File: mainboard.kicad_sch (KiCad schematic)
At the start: 29 parts, among them J1 terminal_led-strip, J2 header_rotary-encoder, J4 header_pi, J5 power_input, J6 AudioJack2, Q1 IRF9540N, SW1 power_switch, U1 OPA2277, U2 MSGEQ7, U4 logic-level-converter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

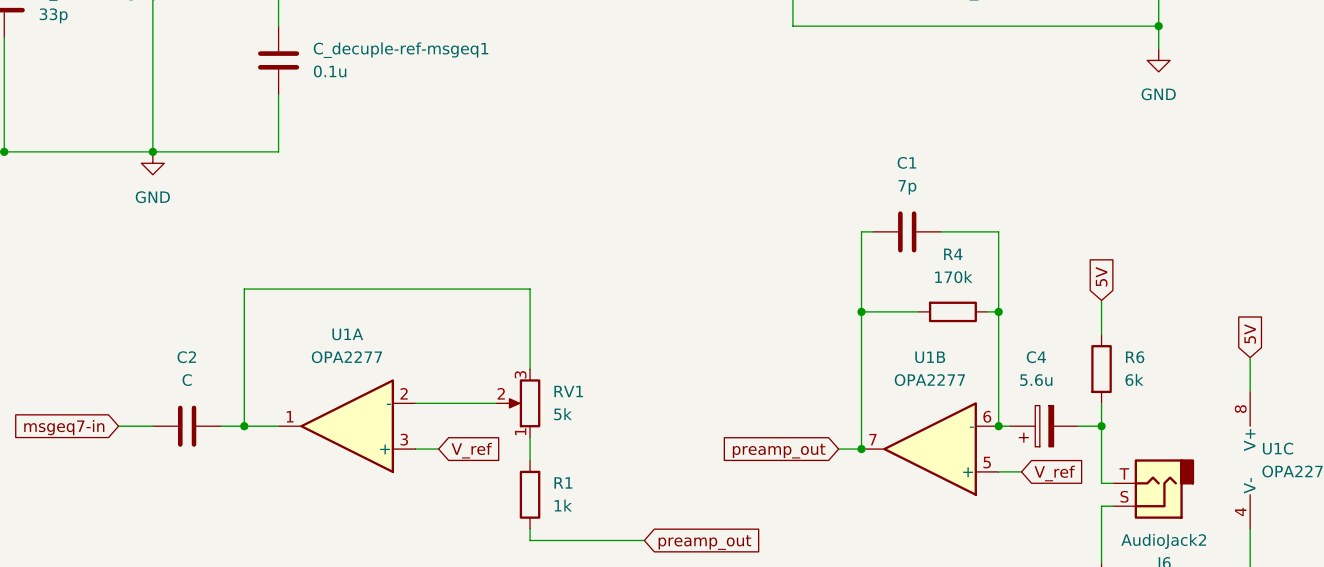
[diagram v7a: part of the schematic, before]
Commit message: add jlc part ids
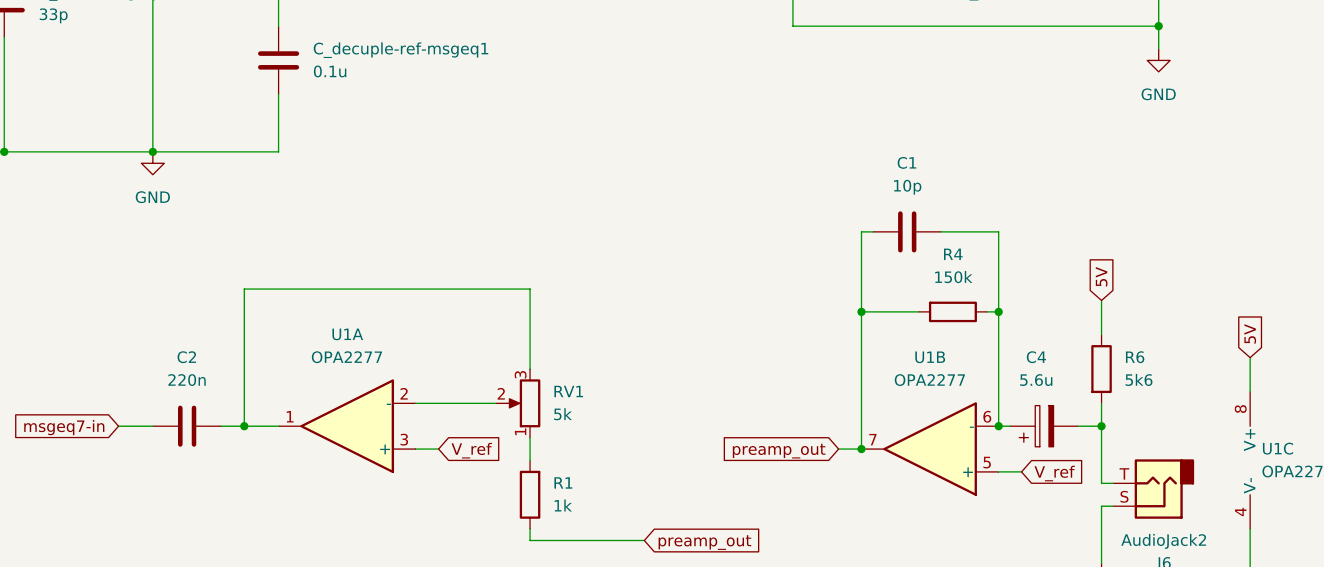
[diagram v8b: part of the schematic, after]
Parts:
- C1: value 7p -> 10p; footprint Capacitor_SMD:C_0805_2012Metric_Pad1.18x1.45mm_HandSolder -> Capacitor_SMD:C_0603_1608Metric_Pad1.08x0.95mm_HandSolder; JLC 0805 -> 0603; LCSC (none) -> C1634
- C2: value C -> 220n; LCSC (none) -> C5378
- C_clock-msgeq1: footprint Capacitor_SMD:C_0805_2012Metric_Pad1.18x1.45mm_HandSolder -> Capacitor_SMD:C_0603_1608Metric_Pad1.08x0.95mm_HandSolder; JLC 0805 -> 0603; LCSC (none) -> C1663
- C_decouple-supply1, C_decuple-ref-msgeq1: LCSC (none) -> C28233
- R1: LCSC (none) -> C17513
- R4: value 170k -> 150k; LCSC (none) -> C17470
- R6: value 6k -> 5k6; LCSC (none) -> C4382
- R_clock-msgeq1: LCSC (none) -> C17539
- R_mosfet1: LCSC (none) -> C17561
- SCL_pullup1, SDA_pullup1: LCSC (none) -> C17604
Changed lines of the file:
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@@
       (effects (font (size 1.27 1.27)) hide)
     )
-    (property "LCSC" "" (at 107.95 45.72 0)
+    (property "LCSC" "C17561" (at 107.95 45.72 0)
       (effects (font (size 1.27 1.27)) hide)
     )
@@
       (effects (font (size 1.27 1.27)) hide)
     )
-    (property "LCSC" "" (at 20.32 87.63 0)
+    (property "LCSC" "C28233" (at 20.32 87.63 0)
       (effects (font (size 1.27 1.27)) hide)
     )
@@
       (effects (font (size 1.27 1.27)) (justify left))
     )
-    (property "Value" "6k" (at 149.86 171.45 0)
+    (property "Value" "5k6" (at 149.86 171.45 0)
       (effects (font (size 1.27 1.27)) (justify left))
     )
@@
       (effects (font (size 1.27 1.27)) hide)
     )
-    (property "LCSC" "" (at 147.32 170.18 0)
+    (property "LCSC" "C4382" (at 147.32 170.18 0)
       (effects (font (size 1.27 1.27)) hide)
     )
@@
       (effects (font (size 1.27 1.27)) hide)
     )
-    (property "LCSC" "" (at 83.82 184.15 0)
+    (property "LCSC" "C17513" (at 83.82 184.15 0)
       (effects (font (size 1.27 1.27)) hide)
     )
@@
       (effects (font (size 1.27 1.27)))
     )
-    (property "Value" "170k" (at 130.81 160.02 90)
+    (property "Value" "150k" (at 130.81 160.02 90)
       (effects (font (size 1.27 1.27)))
     )
@@
       (effects (font (size 1.27 1.27)) hide)
     )
-    (property "LCSC" "" (at 130.81 163.83 0)
+    (property "LCSC" "C17470" (at 130.81 163.83 0)
       (effects (font (size 1.27 1.27)) hide)
     )
@@
       (effects (font (size 1.27 1.27)) hide)
     )
-    (property "LCSC" "" (at 55.88 135.89 0)
+    (property "LCSC" "C28233" (at 55.88 135.89 0)
       (effects (font (size 1.27 1.27)) hide)
     )
@@
       (effects (font (size 1.27 1.27)))
     )
-    (property "Value" "C" (at 45.72 171.45 90)
+    (property "Value" "220n" (at 45.72 171.45 90)
       (effects (font (size 1.27 1.27)))
     )
@@
       (effects (font (size 1.27 1.27)) hide)
     )
-    (property "LCSC" "" (at 45.72 176.53 0)
+    (property "LCSC" "C5378" (at 45.72 176.53 0)
       (effects (font (size 1.27 1.27)) hide)
     )
@@
       (effects (font (size 1.27 1.27)) hide)
     )
-    (property "LCSC" "" (at 162.56 44.45 0)
+    (property "LCSC" "C17604" (at 162.56 44.45 0)
       (effects (font (size 1.27 1.27)) hide)
     )
@@
       (effects (font (size 1.27 1.27)))
     )
-    (property "Value" "7p" (at 125.73 149.86 90)
-      (effects (font (size 1.27 1.27)))
-    )
-    (property "Footprint" "Capacitor_SMD:C_0805_2012Metric_Pad1.18x1.45mm_HandSolder" (at 129.54 153.9748 0)
+    (property "Value" "10p" (at 125.73 149.86 90)
+      (effects (font (size 1.27 1.27)))
+    )
+    (property "Footprint" "Capacitor_SMD:C_0603_1608Metric_Pad1.08x0.95mm_HandSolder" (at 129.54 153.9748 0)
       (effects (font (size 1.27 1.27)) hide)
     )
@@
       (effects (font (size 1.27 1.27)) hide)
     )
-    (property "JLC" "0805" (at 125.73 154.94 0)
-      (effects (font (size 1.27 1.27)) hide)
-    )
-    (property "LCSC" "" (at 125.73 154.94 0)
+    (property "JLC" "0603" (at 125.73 154.94 0)
+      (effects (font (size 1.27 1.27)) hide)
+    )
+    (property "LCSC" "C1634" (at 125.73 154.94 0)
       (effects (font (size 1.27 1.27)) hide)
     )
@@
       (effects (font (size 1.27 1.27)) hide)
     )
-    (property "LCSC" "" (at 25.4 100.33 0)
+    (property "LCSC" "C17539" (at 25.4 100.33 0)
       (effects (font (size 1.27 1.27)) hide)
     )
@@
       (effects (font (size 1.27 1.27)) hide)
     )
-    (property "LCSC" "" (at 151.13 44.45 0)
+    (property "LCSC" "C17604" (at 151.13 44.45 0)
       (effects (font (size 1.27 1.27)) hide)
     )
@@
       (effects (font (size 1.27 1.27)) (justify left))
     )
-    (property "Footprint" "Capacitor_SMD:C_0805_2012Metric_Pad1.18x1.45mm_HandSolder" (at 26.3652 133.35 0)
+    (property "Footprint" "Capacitor_SMD:C_0603_1608Metric_Pad1.08x0.95mm_HandSolder" (at 26.3652 133.35 0)
       (effects (font (size 1.27 1.27)) hide)
     )
@@
       (effects (font (size 1.27 1.27)) hide)
     )
-    (property "JLC" "0805" (at 25.4 129.54 0)
-      (effects (font (size 1.27 1.27)) hide)
-    )
-    (property "LCSC" "" (at 25.4 129.54 0)
-      (effects (font (size 1.27 1.27)) hide)
-    )
+    (property "JLC" "0603" (at 25.4 129.54 0)
+      (effects (font (size 1.27 1.27)) hide)
+    )
+    (property "LCSC" "C1663" (at 25.4 129.54 0)
+      (effects (font (size 1.27 1.27)) hide)
+    )
